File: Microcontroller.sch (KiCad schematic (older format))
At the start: 9 parts

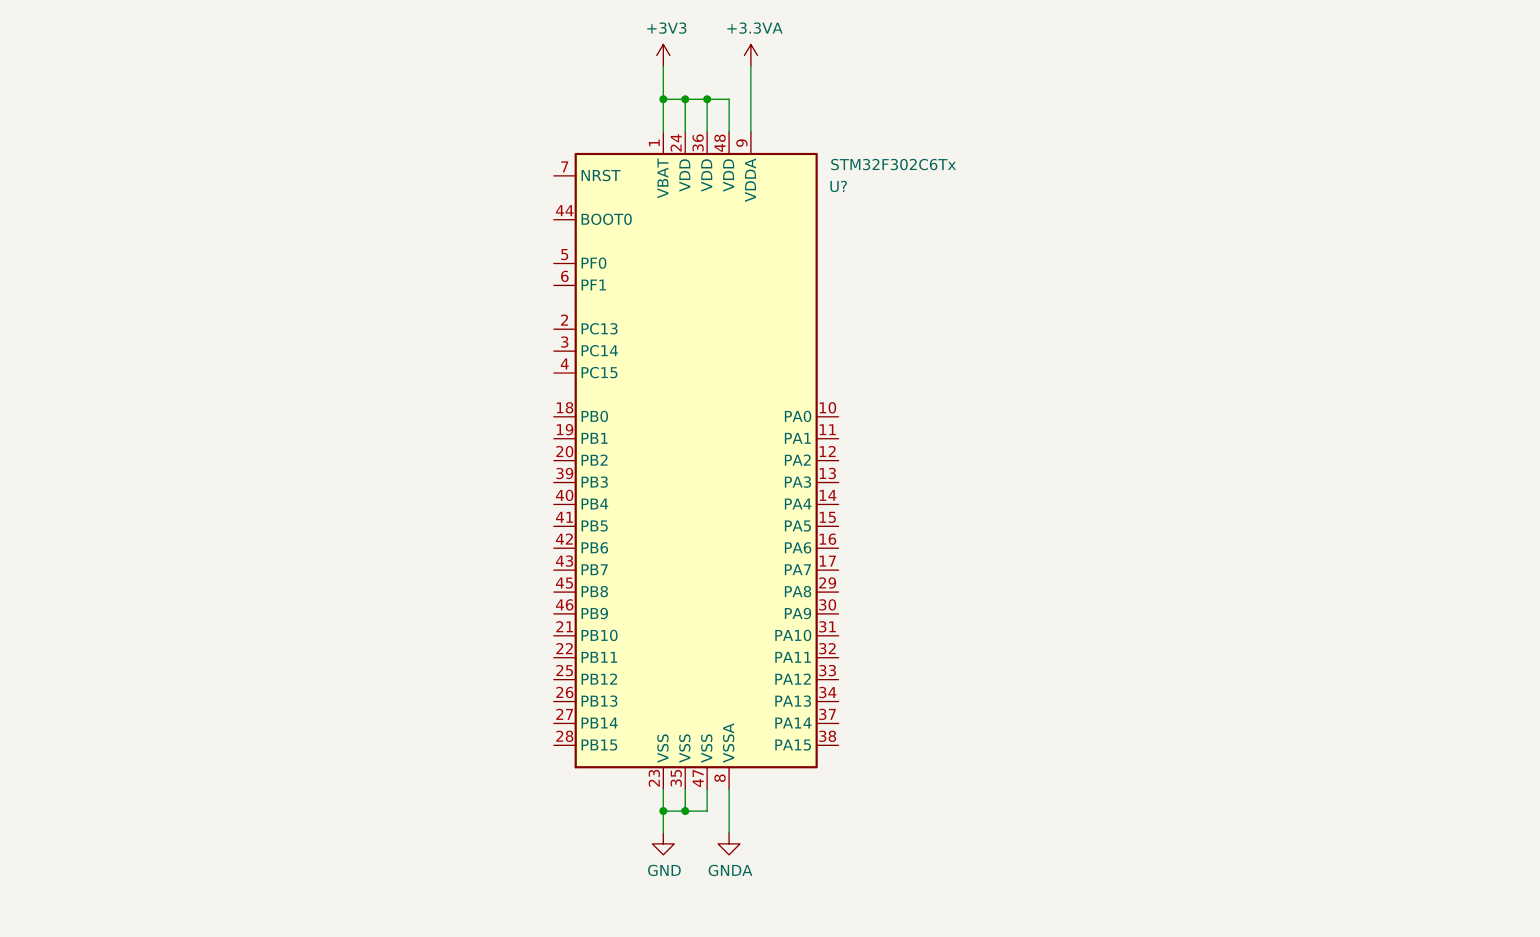
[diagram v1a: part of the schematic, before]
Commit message: Added communication interfaces
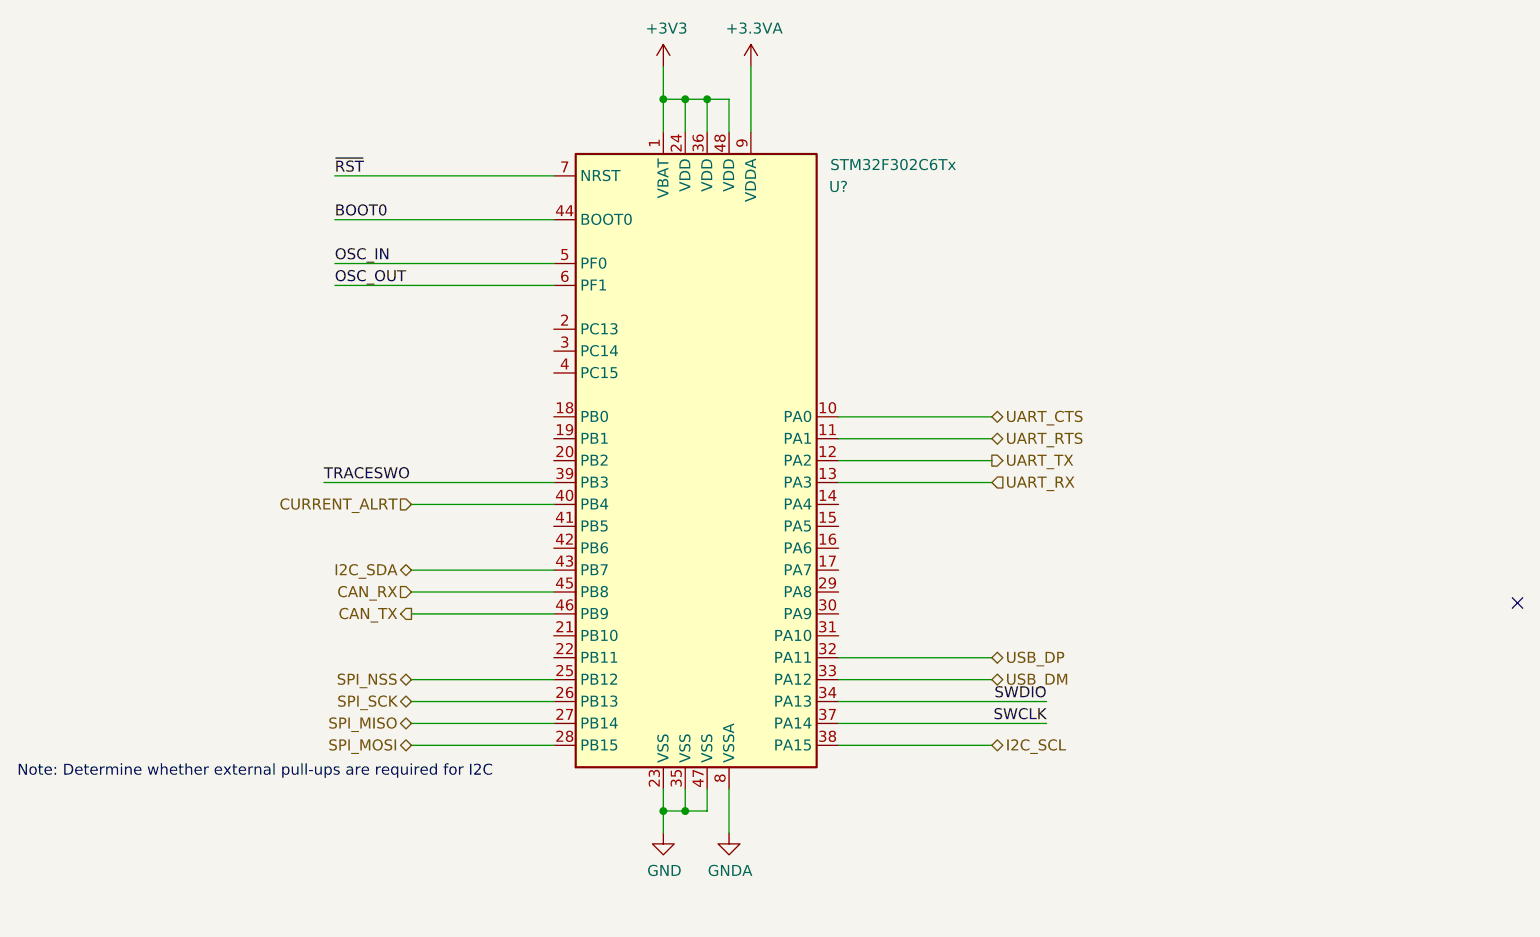
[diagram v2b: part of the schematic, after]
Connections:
- net UART_CTS: now reaches U?.10 (PA0)
- net UART_RTS: now reaches U?.11 (PA1)
- net UART_TX: now reaches U?.12 (PA2)
- net UART_RX: now reaches U?.13 (PA3)
- net SPI_NSS: now reaches U?.25 (PB12)
- net SPI_SCK: now reaches U?.26 (PB13)
- net SPI_MISO: now reaches U?.27 (PB14)
- net SPI_MOSI: now reaches U?.28 (PB15)
- net USB_DP: now reaches U?.32 (PA11)
- net USB_DM: now reaches U?.33 (PA12)
- net SWDIO: now reaches U?.34 (PA13)
- net SWCLK: now reaches U?.37 (PA14)
- net I2C_SCL: now reaches U?.38 (PA15)
- net TRACESWO: now reaches U?.39 (PB3)
- net CURRENT_ALRT: now reaches U?.40 (PB4)
- net I2C_SDA: now reaches U?.43 (PB7)
- net BOOT0: now reaches U?.44 (BOOT0)
- net CAN_RX: now reaches U?.45 (PB8)
- net CAN_TX: now reaches U?.46 (PB9)
- net OSC_IN: now reaches U?.5 (PF0)
- net OSC_OUT: now reaches U?.6 (PF1)
- net ~RST: now reaches U?.7 (NRST)
- no-connect marks 0 -> 1
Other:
- note added: "Note: Determine whether external pull-ups are required for I2C"
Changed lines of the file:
@@
 $Descr A4 11693 8268
 encoding utf-8
-Sheet 1 6
+Sheet 1 1
 Title ""
 Date ""
@@
 Text Notes 3750 6650 0    50   ~ 0
 Microcontroller Decoupling
+Text HLabel 4300 3700 0    50   Input ~ 0
+CURRENT_ALRT
+Text HLabel 4300 4000 0    50   BiDi ~ 0
+I2C_SDA
+Text HLabel 6950 4800 2    50   BiDi ~ 0
+I2C_SCL
+Text Notes 2500 4950 0    50   ~ 0
+Note: Determine whether external pull-ups are required for I2C
+Wire Wire Line
+	6250 4500 6950 4500
+Wire Wire Line
+	6250 4400 6950 4400
+Text HLabel 6950 4400 2    50   BiDi ~ 0
+USB_DP
+Text HLabel 6950 4500 2    50   BiDi ~ 0
+USB_DM
+Text HLabel 4300 4100 0    50   Input ~ 0
+CAN_RX
+Text HLabel 4300 4200 0    50   Output ~ 0
+CAN_TX
+Wire Wire Line
+	4300 4200 4950 4200
+Wire Wire Line
+	4300 4100 4950 4100
+Wire Wire Line
+	4300 3700 4950 3700
+Wire Wire Line
+	4950 3600 3900 3600
+Text Label 3900 3600 0    50   ~ 0
+TRACESWO
+Wire Wire Line
+	6250 4700 7200 4700
+Text Label 7200 4700 2    50   ~ 0
+SWCLK
+Wire Wire Line
+	6250 4600 7200 4600
+Text Label 7200 4600 2    50   ~ 0
+SWDIO
+Wire Wire Line
+	6250 3300 6950 3300
+Text HLabel 6950 3500 2    50   Output ~ 0
+UART_TX
+Text HLabel 6950 3600 2    50   Input ~ 0
+UART_RX
+Wire Wire Line
+	6250 3400 6950 3400
+Wire Wire Line
+	6950 3500 6250 3500
+Wire Wire Line
+	6250 3600 6950 3600
+Text HLabel 6950 3400 2    50   BiDi ~ 0
+UART_RTS
+Text HLabel 6950 3300 2    50   BiDi ~ 0
+UART_CTS
+Wire Wire Line
+	4950 2200 3950 2200
+Text Label 3950 2200 0    50   ~ 0
+~RST
+Wire Wire Line
+	4950 2600 3950 2600
+Text Label 3950 2600 0    50   ~ 0
+OSC_IN
+Wire Wire Line
+	4950 2700 3950 2700
+Text Label 3950 2700 0    50   ~ 0
+OSC_OUT
+Wire Wire Line
+	4950 2400 3950 2400
+Text Label 3950 2400 0    50   ~ 0
+BOOT0
+NoConn ~ 9350 4150
+Wire Wire Line
+	4300 4000 4950 4000
+Wire Wire Line
+	6250 4800 6950 4800
+Wire Wire Line
+	4300 4800 4950 4800
+Wire Wire Line
+	4950 4700 4300 4700
+Wire Wire Line
+	4950 4600 4300 4600
+Text HLabel 4300 4600 0    50   BiDi ~ 0
+SPI_SCK
+Text HLabel 4300 4700 0    50   BiDi ~ 0
+SPI_MISO
+Text HLabel 4300 4800 0    50   BiDi ~ 0
+SPI_MOSI
+Wire Wire Line
+	4300 4500 4950 4500
+Text HLabel 4300 4500 0    50   BiDi ~ 0
+SPI_NSS
 $EndSCHEMATC

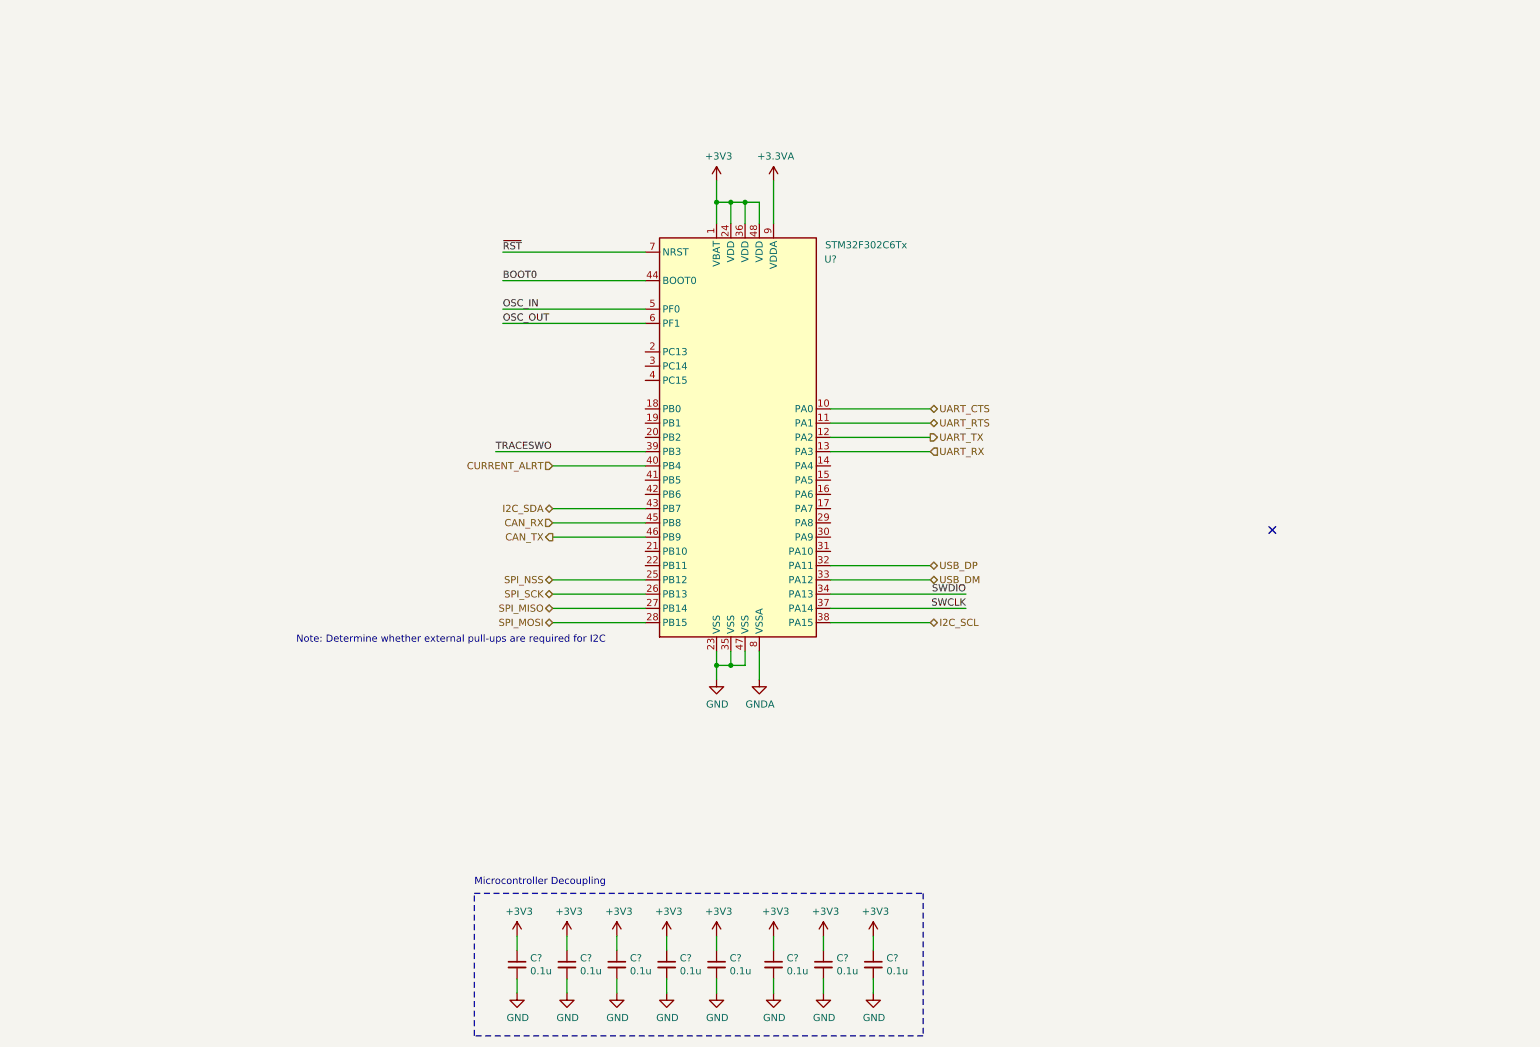
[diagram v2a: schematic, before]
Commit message: Added I2C Pullup Resistors
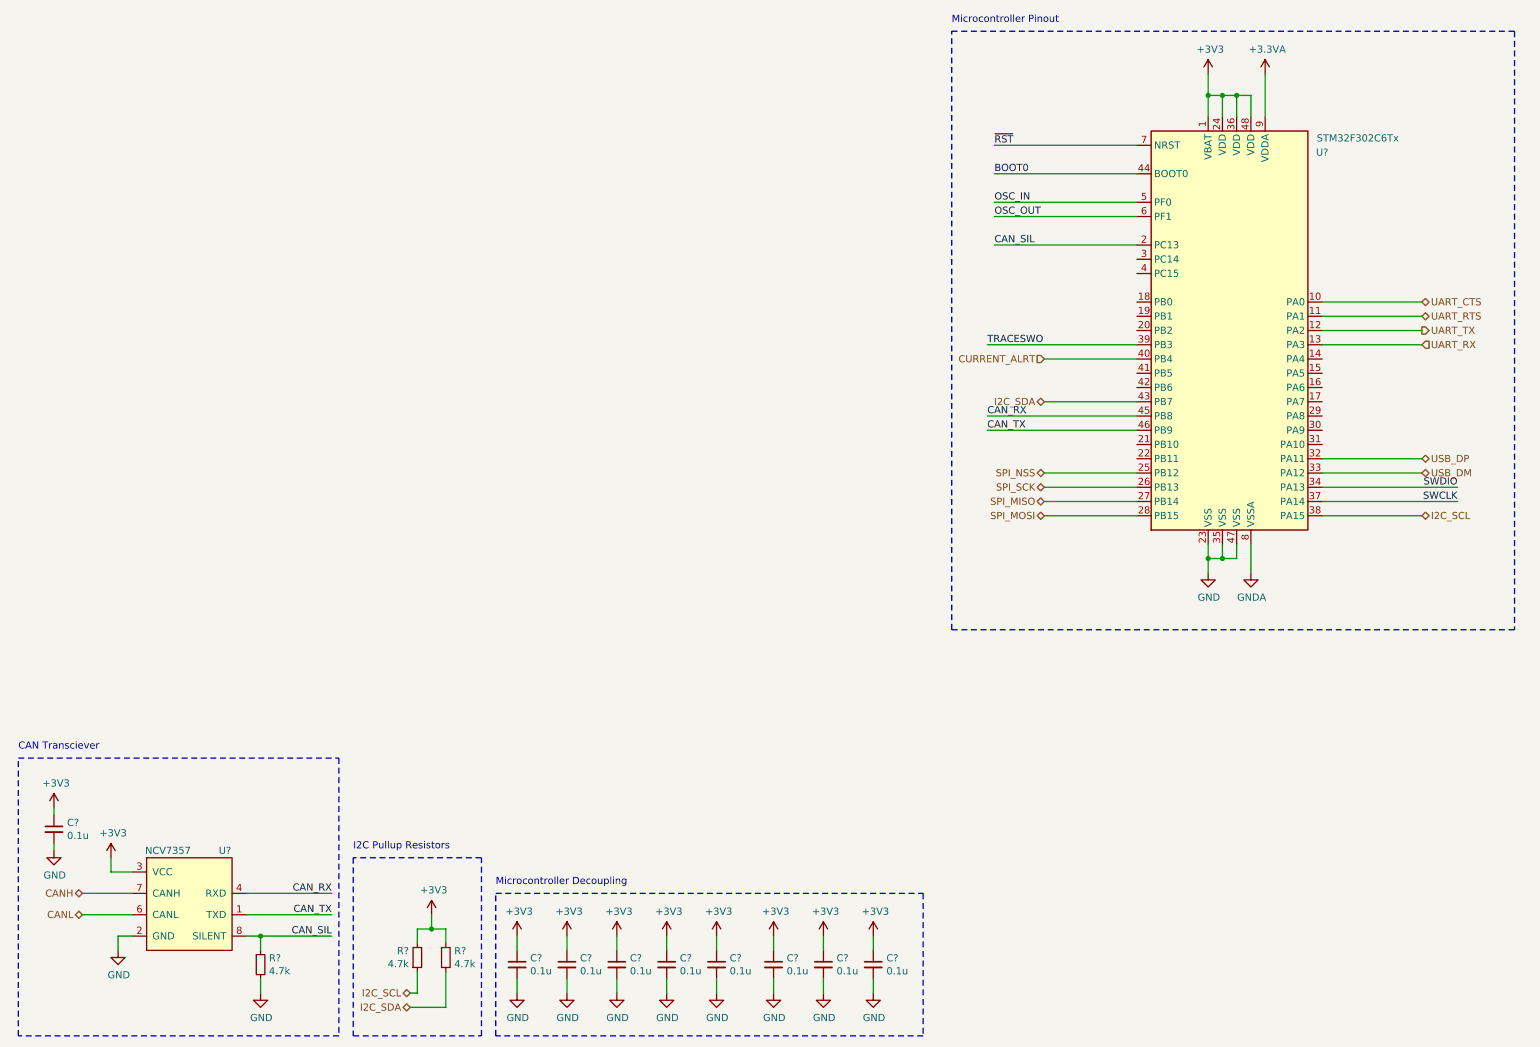
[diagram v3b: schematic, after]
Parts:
- added C?: 0.1u, Capacitor_SMD:C_0603_1608Metric, symbol Device:C_Small
- added R? (x3): 4.7k, symbol Device:R_Small
- added U?: NCV7357, symbol ReflowOven:NCV7357
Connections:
- net +3V3: now also C?.1, R?.1, R?.2, U?.3 (VCC)
- net CAN_RX: now also U?.4 (RXD)
- net CAN_TX: now also U?.1 (TXD)
- net GND: now also C?.2, R?.2, U?.2 (GND)
- net I2C_SCL: now also R?.1
- net I2C_SDA: now also R?.2
- net CAN_SIL: now reaches U?.2 (PC13)
- net CAN_SIL: now also R?.1, U?.8 (SILENT)
- new net CANH: U?.7 (CANH)
- new net CANL: U?.6 (CANL)
- no-connect marks 1 -> 0
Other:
- note added: "CAN Transciever"
- note added: "I2C Pullup Resistors"
- note added: "Microcontroller Pinout"
- note removed: "Note: Determine whether external pull-ups are required for I2C"
- moved on the sheet: U?

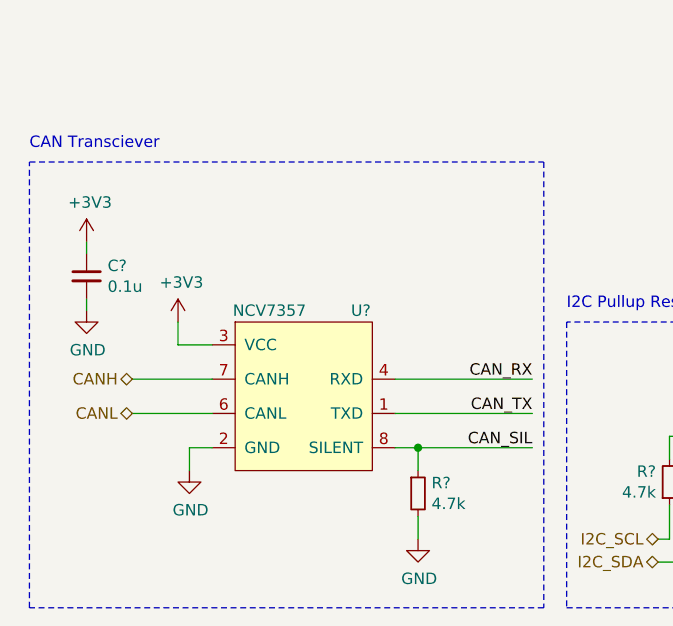
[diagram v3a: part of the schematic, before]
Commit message: Added current sense
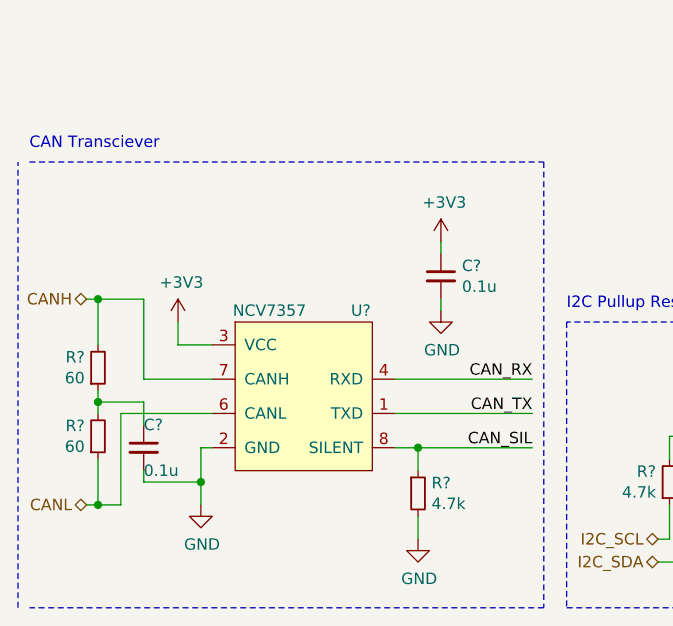
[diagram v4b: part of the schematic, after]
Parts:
- added C?: 0.1u, Capacitor_SMD:C_0603_1608Metric, symbol Device:C_Small
- added R? (x2): 60, symbol Device:R_Small
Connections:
- net CANH: now also R?.2
- net CANL: now also R?.1
- net GND: now also C?.2
- new net: C?.1, R?.1, R?.2
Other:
- moved on the sheet: C?
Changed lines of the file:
@@
-	1    0    0    -1
-$EndComp
-Wire Wire Line
-	1350 7000 1250 7000
-Wire Wire Line
-	1250 7000 1250 7100
-$Comp
-L power:GND #PWR?
-U 1 1 5F6C9398
-P 1250 7100
-F 0 "#PWR?" H 1250 6850 50  0001 C CNN
-F 1 "GND" H 1255 6927 50  0000 C CNN
-F 2 "" H 1250 7100 50  0001 C CNN
-F 3 "" H 1250 7100 50  0001 C CNN
-	1    1250 7100
 	1    0    0    -1
 $EndComp
@@
 Wire Wire Line
 	1200 6550 1350 6550
-Wire Wire Line
-	1350 6700 1000 6700
-Wire Wire Line
-	1350 6850 1000 6850
-Text HLabel 1000 6700 0    50   BiDi ~ 0
-CANH
-Text HLabel 1000 6850 0    50   BiDi ~ 0
+Text HLabel 800  7250 0    50   BiDi ~ 0
 CANL
 $Comp
 L power:+3V3 #PWR?
 U 1 1 5F6D6BB3
-P 800 6100
-F 0 "#PWR?" H 800 5950 50  0001 C CNN
-F 1 "+3V3" H 815 6273 50  0000 C CNN
-F 2 "" H 800 6100 50  0001 C CNN
-F 3 "" H 800 6100 50  0001 C CNN
-	1    800  6100
+P 2350 6100
+F 0 "#PWR?" H 2350 5950 50  0001 C CNN
+F 1 "+3V3" H 2365 6273 50  0000 C CNN
+F 2 "" H 2350 6100 50  0001 C CNN
+F 3 "" H 2350 6100 50  0001 C CNN
+	1    2350 6100
 	1    0    0    -1
 $EndComp
@@
 L Device:C_Small C?
 U 1 1 5F6D6BB9
-P 800 6250
-F 0 "C?" H 892 6296 50  0000 L CNN
-F 1 "0.1u" H 892 6205 50  0000 L CNN
-F 2 "Capacitor_SMD:C_0603_1608Metric" H 800 6250 50  0001 C CNN
-F 3 "~" H 800 6250 50  0001 C CNN
-	1    800  6250
+P 2350 6250
+F 0 "C?" H 2442 6296 50  0000 L CNN
+F 1 "0.1u" H 2442 6205 50  0000 L CNN
+F 2 "Capacitor_SMD:C_0603_1608Metric" H 2350 6250 50  0001 C CNN
+F 3 "~" H 2350 6250 50  0001 C CNN
+	1    2350 6250
 	1    0    0    -1
 $EndComp
@@
 L power:GND #PWR?
 U 1 1 5F6D6BBF
-P 800 6400
-F 0 "#PWR?" H 800 6150 50  0001 C CNN
-F 1 "GND" H 805 6227 50  0000 C CNN
-F 2 "" H 800 6400 50  0001 C CNN
-F 3 "" H 800 6400 50  0001 C CNN
-	1    800  6400
-	1    0    0    -1
-$EndComp
-Wire Wire Line
-	800  6400 800  6350
-Wire Wire Line
-	800  6150 800  6100
+P 2350 6400
+F 0 "#PWR?" H 2350 6150 50  0001 C CNN
+F 1 "GND" H 2355 6227 50  0000 C CNN
+F 2 "" H 2350 6400 50  0001 C CNN
+F 3 "" H 2350 6400 50  0001 C CNN
+	1    2350 6400
+	1    0    0    -1
+$EndComp
+Wire Wire Line
+	2350 6400 2350 6350
+Wire Wire Line
+	2350 6150 2350 6100
 Wire Wire Line
 	8400 3350 7350 3350
@@
 	2800 7700 550  7700
 Wire Notes Line
-	550  7700 550  5750
+	500  7700 500  5750
 Wire Notes Line
 	550  5750 2800 5750
@@
 Text Notes 2900 6400 0    50   ~ 0
 I2C Pullup Resistors
+$Comp
+L Device:R_Small R?
+U 1 1 5F74CF4E
+P 850 6650
+F 0 "R?" H 792 6604 50  0000 R CNN
+F 1 "60" H 792 6695 50  0000 R CNN
+F 2 "" H 850 6650 50  0001 C CNN
+F 3 "~" H 850 6650 50  0001 C CNN
+	1    850  6650
+	1    0    0    1
+$EndComp
+$Comp
+L Device:R_Small R?
+U 1 1 5F74D653
+P 850 6950
+F 0 "R?" H 792 6904 50  0000 R CNN
+F 1 "60" H 792 6995 50  0000 R CNN
+F 2 "" H 850 6950 50  0001 C CNN
+F 3 "~" H 850 6950 50  0001 C CNN
+	1    850  6950
+	1    0    0    1
+$EndComp
+Wire Wire Line
+	1350 7000 1300 7000
+Wire Wire Line
+	1050 6800 850  6800
+Wire Wire Line
+	850  6800 850  6750
+Wire Wire Line
+	850  6800 850  6850
+Connection ~ 850  6800
+Wire Wire Line
+	800  6350 850  6350
+Wire Wire Line
+	850  6350 850  6550
+Wire Wire Line
+	800  7250 850  7250
+Wire Wire Line
+	850  7250 850  7050
+Text HLabel 800  6350 0    50   BiDi ~ 0
+CANH
+Wire Wire Line
+	1050 6900 1050 6800
+$Comp
+L Device:C_Small C?
+U 1 1 5F7517A6
+P 1050 7000
+F 0 "C?" H 1050 7100 50  0000 L CNN
+F 1 "0.1u" H 1050 6900 50  0000 L CNN
+F 2 "Capacitor_SMD:C_0603_1608Metric" H 1050 7000 50  0001 C CNN
+F 3 "~" H 1050 7000 50  0001 C CNN
+	1    1050 7000
+	1    0    0    -1
+$EndComp
+Wire Wire Line
+	1050 7150 1050 7100
+$Comp
+L power:GND #PWR?
+U 1 1 5F6C9398
+P 1300 7250
+F 0 "#PWR?" H 1300 7000 50  0001 C CNN
+F 1 "GND" H 1305 7077 50  0000 C CNN
+F 2 "" H 1300 7250 50  0001 C CNN
+F 3 "" H 1300 7250 50  0001 C CNN
+	1    1300 7250
+	1    0    0    -1
+$EndComp
+Wire Wire Line
+	1300 7250 1300 7150
+Wire Wire Line
+	1300 7000 1300 7150
+Connection ~ 1300 7150
+Wire Wire Line
+	1050 7150 1300 7150
+Wire Wire Line
+	850  6350 1050 6350
+Wire Wire Line
+	1050 6350 1050 6700
+Wire Wire Line
+	1050 6700 1350 6700
+Connection ~ 850  6350
+Wire Wire Line
+	850  7250 950  7250
+Connection ~ 850  7250
+Wire Wire Line
+	950  7250 950  6850
+Wire Wire Line
+	950  6850 1350 6850
 $EndSCHEMATC
